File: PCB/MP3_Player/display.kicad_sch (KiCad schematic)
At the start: 8 parts, among them Q1 S8050

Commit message: Minor Schematic Changes
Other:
- moved on the sheet: Q1, R11, R12, R13, TP11

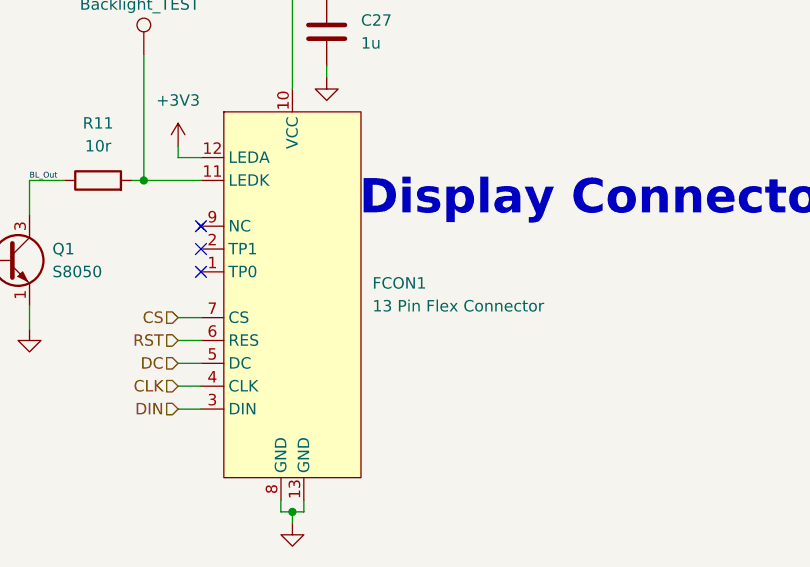
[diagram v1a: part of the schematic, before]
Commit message: Started Making BOM
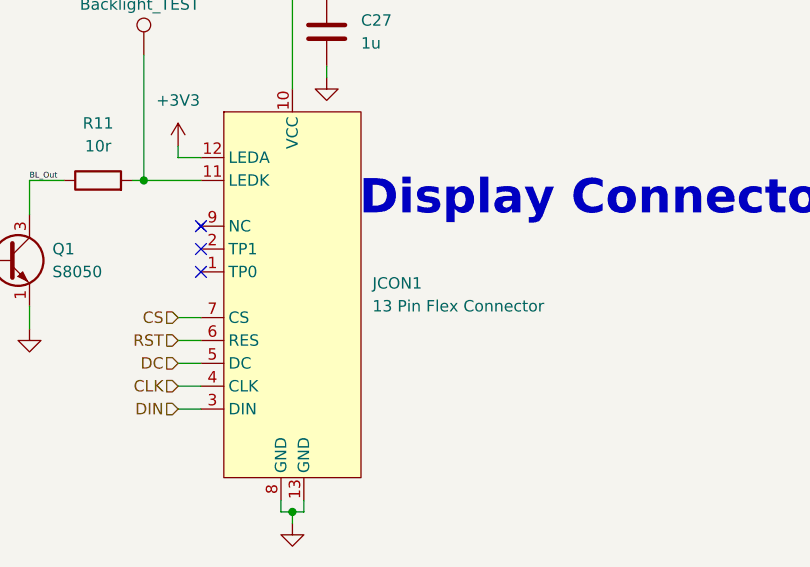
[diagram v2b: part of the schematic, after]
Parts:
- C27: Mfr. Part # (none) -> CL05A105MQ5NNND; Store URL - Digikey (none) -> https://www.digikey.pt/pt/products/detail/samsung-electro-m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; Store URL - Mouser (none) -> https://pt.mouser.com/en/ProductDetail/Samsung-Electro-Mech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
- Q1: Mfr. Part # (none) -> S8050; Store URL - Digikey (none) -> https://www.digikey.pt/pt/products/detail/guangdong-inmark-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
- TP11: now left out of the parts list
- renumbered FCON1 to JCON1

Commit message: Continue Making BOM
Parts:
- DSP1: Mfr. Part # (none) -> TST09602A
- JCON1: Mfr. Part # (none) -> IMSA-9640S-13Y900; Store URL - Digikey (none) -> https://www.digikey.pt/pt/products/detail/iriso/IMSA-9640S-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
- Q1: footprint Package_TO_SOT_THT:TO-92_Inline -> (none); Store URL - Mouser (none) -> https://pt.mouser.com/en/ProductDetail/Comchip-Technology/S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
- R11: Mfr. Part # (none) -> CRCW060310R0FKEA; Store URL - Digikey (none) -> https://www.digikey.pt/pt/products/detail/vishay-dale/CRCW0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; Store URL - Mouser (none) -> https://pt.mouser.com/en/ProductDetail/Vishay/CRCW060310R0F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
- R12: Mfr. Part # (none) -> CRCW040210K0FKED; Store URL - Digikey (none) -> https://www.digikey.pt/pt/products/detail/vishay-dale/CRCW0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; Store URL - Mouser (none) -> https://pt.mouser.com/en/ProductDetail/Vishay/CRCW040210K0F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
- R13: Mfr. Part # (none) -> CRCW04021K00FKED; Store URL - Digikey (none) -> https://www.digikey.pt/pt/products/detail/vishay-dale/CRCW0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; Store URL - Mouser (none) -> https://pt.mouser.com/en/ProductDetail/Vishay/CRCW04021K00F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
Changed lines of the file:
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@@
 			)
 		)
-		(property "Datasheet" ""
+		(property "Datasheet" "https://www.panelook.com/TST09602A-0-96inch-IPS-TFT-LCD-screen-80-160-350cd-m-sup2-13PINS-SPI-ST7735S-Wearable-LCD-detail_134063.html"
 			(at 77.47 133.35 0)
 			(hide yes)
@@
 			)
 		)
-		(property "Description" ""
+		(property "Description" "0.96 inch IPS TFT LCD screen 80x160 350cd/m² 13PINS SPI ST7735S"
 			(at 77.47 137.16 0)
 			(hide yes)
@@
 		)
 		(property "Store URL - TME" ""
+			(at 77.47 137.16 0)
+			(hide yes)
+			(show_name no)
+			(do_not_autoplace no)
+			(effects
+				(font
+					(size 1.27 1.27)
+				)
+			)
+		)
+		(property "Mfr. Part #" "TST09602A"
 			(at 77.47 137.16 0)
 			(hide yes)
@@
 			)
 		)
-		(property "Datasheet" ""
+		(property "Datasheet" "https://www.irisoconnectors.com/system/cms/assets/uploads/files/spec-sheets/product/original/is-9640a-1.pdf?1543584151"
 			(at 154.94 100.33 0)
 			(hide yes)
@@
 			)
 		)
-		(property "Description" "0.96 inch IPS TFT LCD screen 80x160 350cd/m² 13PINS SPI ST7735S"
+		(property "Description" "13 Pin 0.4mm Pitch"
 			(at 156.464 135.89 0)
 			(hide yes)
@@
 		)
 		(property "Store URL - TME" ""
+			(at 154.94 100.33 0)
+			(hide yes)
+			(show_name no)
+			(do_not_autoplace no)
+			(effects
+				(font
+					(size 1.27 1.27)
+				)
+			)
+		)
+		(property "Mfr. Part #" "IMSA-9640S-13Y900"
+			(at 154.94 100.33 0)
+			(hide yes)
+			(show_name no)
+			(do_not_autoplace no)
+			(effects
+				(font
+					(size 1.27 1.27)
+				)
+			)
+		)
+		(property "Store URL - Digikey" "https://www.digikey.pt/pt/products/detail/iriso/IMSA-9640S-13Y900/26774114"
 			(at 154.94 100.33 0)
 			(hide yes)
@@
 			)
 		)
-		(property "Datasheet" ""
+		(property "Datasheet" "https://www.vishay.com/docs/20035/dcrcwe3.pdf"
 			(at 114.3 90.17 0)
 			(hide yes)
@@
 			)
 		)
-		(property "Description" "Resistor"
+		(property "Description" "0402"
 			(at 114.3 90.17 0)
 			(hide yes)
@@
 		)
 		(property "Store URL - TME" ""
+			(at 114.3 90.17 0)
+			(hide yes)
+			(show_name no)
+			(do_not_autoplace no)
+			(effects
+				(font
+					(size 1.27 1.27)
+				)
+			)
+		)
+		(property "Mfr. Part #" "CRCW040210K0FKED"
+			(at 114.3 90.17 0)
+			(hide yes)
+			(show_name no)
+			(do_not_autoplace no)
+			(effects
+				(font
+					(size 1.27 1.27)
+				)
+			)
+		)
+		(property "Store URL - Digikey" "https://www.digikey.pt/pt/products/detail/vishay-dale/CRCW040210K0FKED/1178121"
+			(at 114.3 90.17 0)
+			(hide yes)
+			(show_name no)
+			(do_not_autoplace no)
+			(effects
+				(font
+					(size 1.27 1.27)
+				)
+			)
+		)
+		(property "Store URL - Mouser" "https://pt.mouser.com/en/ProductDetail/Vishay/CRCW040210K0FKED?qs=rlE3Te1NifyN3e8vvxacSw%3D%3D"
 			(at 114.3 90.17 0)
 			(hide yes)
@@
 			)
 		)
-		(property "Footprint" "Package_TO_SOT_THT:TO-92_Inline"
+		(property "Footprint" ""
 			(at 128.27 98.425 0)
 			(hide yes)
@@
 			)
 		)
-		(property "Description" "0.7A Ic, 20V Vce, Low Voltage High Current NPN Transistor, TO-92"
+		(property "Description" "0.7A Ic, 20V Vce, Low Voltage High Current NPN Transistor, SOT-23"
 			(at 123.19 96.52 0)
 			(hide yes)
@@
 		)
 		(property "Store URL - Digikey" "https://www.digikey.pt/pt/products/detail/guangdong-inmark-electronics-co-ltd/S8050/28538968"
+			(at 123.19 96.52 0)
+			(hide yes)
+			(show_name no)
+			(do_not_autoplace no)
+			(effects
+				(font
+					(size 1.27 1.27)
+				)
+			)
+		)
+		(property "Store URL - Mouser" "https://pt.mouser.com/en/ProductDetail/Comchip-Technology/SS8050-G?qs=LLUE9lz1YbcHg%252BWLMAtcrQ%3D%3D"
 			(at 123.19 96.52 0)
 			(hide yes)
@@
 			)
 		)
-		(property "Datasheet" ""
+		(property "Datasheet" "https://www.vishay.com/docs/20035/dcrcwe3.pdf"
 			(at 102.87 96.52 0)
 			(hide yes)
@@
 			)
 		)
-		(property "Description" "Resistor"
+		(property "Description" "0402"
 			(at 102.87 96.52 0)
 			(hide yes)
@@
 		)
 		(property "Store URL - TME" ""
+			(at 102.87 96.52 90)
+			(hide yes)
+			(show_name no)
+			(do_not_autoplace no)
+			(effects
+				(font
+					(size 1.27 1.27)
+				)
+			)
+		)
+		(property "Mfr. Part #" "CRCW04021K00FKED"
+			(at 102.87 96.52 90)
+			(hide yes)
+			(show_name no)
+			(do_not_autoplace no)
+			(effects
+				(font
+					(size 1.27 1.27)
+				)
+			)
+		)
+		(property "Store URL - Digikey" "https://www.digikey.pt/pt/products/detail/vishay-dale/CRCW04021K00FKED/1178007"
+			(at 102.87 96.52 90)
+			(hide yes)
+			(show_name no)
+			(do_not_autoplace no)
+			(effects
+				(font
+					(size 1.27 1.27)
+				)
+			)
+		)
+		(property "Store URL - Mouser" "https://pt.mouser.com/en/ProductDetail/Vishay/CRCW04021K00FKED?qs=YX%252BK5oaHNYqQ2WK%252BIAW12A%3D%3D"
 			(at 102.87 96.52 90)
 			(hide yes)
@@
 			)
 		)
-		(property "Datasheet" ""
+		(property "Datasheet" "https://www.vishay.com/docs/20035/dcrcwe3.pdf"
 			(at 133.35 87.63 0)
 			(hide yes)
@@
 			)
 		)
-		(property "Description" "Resistor"
+		(property "Description" "0603"
 			(at 133.35 87.63 0)
 			(hide yes)
@@
 			(at 133.35 87.63 90)
 			(hide yes)
+			(show_name no)
+			(do_not_autoplace no)
+			(effects
+				(font
+					(size 1.27 1.27)
+				)
+			)
+		)
+		(property "Mfr. Part #" "CRCW060310R0FKEA"
+			(at 133.35 87.63 90)
+			(hide yes)
+			(show_name no)
+			(do_not_autoplace no)
+			(effects
+				(font
+					(size 1.27 1.27)
+				)
+			)
+		)
+		(property "Store URL - Digikey" "https://www.digikey.pt/pt/products/detail/vishay-dale/CRCW060310R0FKEA/1174440"
+			(at 133.35 87.63 90)
+			(hide yes)
+			(show_name no)
+			(do_not_autoplace no)
+			(effects
+				(font
+					(size 1.27 1.27)
+				)
+			)
+		)
+		(property "Store URL - Mouser" "https://pt.mouser.com/en/ProductDetail/Vishay/CRCW060310R0FKEA?qs=wiO5jjUX9wsETsRLGnHNyA%3D%3D"
+			(at 133.35 87.63 90)
+			(hide yes)

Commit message: Finished BOM; Started Footprint assignment
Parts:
- C27, R12, R13: footprint (none) -> Capacitor_SMD:C_0402_1005Metric
- DSP1: footprint (none) -> N/A; Store URL - Digikey (none) -> N/A; Store URL - Mouser (none) -> N/A
- JCON1: Mfr. Part # IMSA-9640S-13Y900 -> TF29-13S-0.4SH(800); Store URL - Digikey https://www.digikey.pt/pt/products/detail/iriso/IMSA-9640S-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 -> https://www.digikey.pt/pt/products/detail/hirose-electric-c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; Store URL - Mouser (none) -> https://pt.mouser.com/en/ProductDetail/Hirose-Connector/TF2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
- R11: footprint (none) -> Capacitor_SMD:C_0603_1608Metric
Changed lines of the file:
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@@
 			)
 		)
-		(property "Footprint" ""
+		(property "Footprint" "N/A"
 			(at 77.47 143.51 0)
 			(hide yes)
@@
 		)
 		(property "Mfr. Part #" "TST09602A"
+			(at 77.47 137.16 0)
+			(hide yes)
+			(show_name no)
+			(do_not_autoplace no)
+			(effects
+				(font
+					(size 1.27 1.27)
+				)
+			)
+		)
+		(property "Store URL - Digikey" "N/A"
+			(at 77.47 137.16 0)
+			(hide yes)
+			(show_name no)
+			(do_not_autoplace no)
+			(effects
+				(font
+					(size 1.27 1.27)
+				)
+			)
+		)
+		(property "Store URL - Mouser" "N/A"
 			(at 77.47 137.16 0)
 			(hide yes)
@@
 			)
 		)
-		(property "Datasheet" "https://www.irisoconnectors.com/system/cms/assets/uploads/files/spec-sheets/product/original/is-9640a-1.pdf?1543584151"
+		(property "Datasheet" "https://www.hirose.com/product/document?clcode=CL0480-0514-0-00&productname=TF29-13S-0.4SH(800)&series=TF29&documenttype=Catalog&lang=en&documentid=D167191_en"
 			(at 154.94 100.33 0)
 			(hide yes)
@@
 			)
 		)
-		(property "Mfr. Part #" "IMSA-9640S-13Y900"
+		(property "Mfr. Part #" "TF29-13S-0.4SH(800)"
 			(at 154.94 100.33 0)
 			(hide yes)
@@
 			)
 		)
-		(property "Store URL - Digikey" "https://www.digikey.pt/pt/products/detail/iriso/IMSA-9640S-13Y900/26774114"
+		(property "Store URL - Digikey" "https://www.digikey.pt/pt/products/detail/hirose-electric-co-ltd/TF29-13S-0-4SH-800/11204980?s=N4IgTCBcDaICoDEwE4C0BGAzAZVQBgDoAWbACQAoAOPPAShAF0BfIA"
+			(at 154.94 100.33 0)
+			(hide yes)
+			(show_name no)
+			(do_not_autoplace no)
+			(effects
+				(font
+					(size 1.27 1.27)
+				)
+			)
+		)
+		(property "Store URL - Mouser" "https://pt.mouser.com/en/ProductDetail/Hirose-Connector/TF29-13S-0.4SH800?qs=T3oQrply3y8YJrVVdrUYPw%3D%3D"
 			(at 154.94 100.33 0)
 			(hide yes)
@@
 			)
 		)
-		(property "Footprint" ""
+		(property "Footprint" "Capacitor_SMD:C_0402_1005Metric"
 			(at 159.7152 74.93 0)
 			(hide yes)
@@
 			)
 		)
-		(property "Footprint" ""
+		(property "Footprint" "Capacitor_SMD:C_0402_1005Metric"
 			(at 116.078 90.17 90)
 			(hide yes)
@@
 			)
 		)
-		(property "Footprint" ""
+		(property "Footprint" "Capacitor_SMD:C_0402_1005Metric"
 			(at 102.87 98.298 90)
 			(hide yes)
@@
 			)
 		)
-		(property "Footprint" ""
+		(property "Footprint" "Capacitor_SMD:C_0603_1608Metric"
 			(at 133.35 89.408 90)
 			(hide yes)

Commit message: Footprint Assingment
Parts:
- Q1: footprint (none) -> Package_TO_SOT_SMD:TSOT-23
- R11: footprint Capacitor_SMD:C_0603_1608Metric -> Resistor_SMD:R_0603_1608Metric
- R12, R13: footprint Capacitor_SMD:C_0402_1005Metric -> Resistor_SMD:R_0402_1005Metric
- TP11: footprint (none) -> TestPoint:TestPoint_Pad_D1.5mm
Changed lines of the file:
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@@
 			)
 		)
-		(property "Footprint" ""
+		(property "Footprint" "TestPoint:TestPoint_Pad_D1.5mm"
 			(at 143.51 73.66 0)
 			(hide yes)
@@
 			)
 		)
-		(property "Footprint" "Capacitor_SMD:C_0402_1005Metric"
+		(property "Footprint" "Resistor_SMD:R_0402_1005Metric"
 			(at 116.078 90.17 90)
 			(hide yes)
@@
 			)
 		)
-		(property "Footprint" ""
+		(property "Footprint" "Package_TO_SOT_SMD:TSOT-23"
 			(at 128.27 98.425 0)
 			(hide yes)
@@
 			)
 		)
-		(property "Footprint" "Capacitor_SMD:C_0402_1005Metric"
+		(property "Footprint" "Resistor_SMD:R_0402_1005Metric"
 			(at 102.87 98.298 90)
 			(hide yes)
@@
 			)
 		)
-		(property "Footprint" "Capacitor_SMD:C_0603_1608Metric"
+		(property "Footprint" "Resistor_SMD:R_0603_1608Metric"
 			(at 133.35 89.408 90)
 			(hide yes)

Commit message: Footprint Assingment Complete
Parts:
- JCON1: footprint (none) -> TF29-13S-0.4SH(800):HRS_TF29-13S-0.4SH_800_
- TP11: footprint TestPoint:TestPoint_Pad_D1.5mm -> TestPoint:TestPoint_Pad_D1.0mm
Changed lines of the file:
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@@
 			)
 		)
-		(property "Footprint" ""
+		(property "Footprint" "TF29-13S-0.4SH(800):HRS_TF29-13S-0.4SH_800_"
 			(at 154.94 100.33 0)
 			(hide yes)
@@
 			)
 		)
-		(property "Footprint" "TestPoint:TestPoint_Pad_D1.5mm"
+		(property "Footprint" "TestPoint:TestPoint_Pad_D1.0mm"
 			(at 143.51 73.66 0)
 			(hide yes)

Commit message: PCB Routing
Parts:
- DSP1: Mfr. Part # TST09602A -> (none)
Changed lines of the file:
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@@
 			)
 		)
-		(property "Datasheet" "https://www.panelook.com/TST09602A-0-96inch-IPS-TFT-LCD-screen-80-160-350cd-m-sup2-13PINS-SPI-ST7735S-Wearable-LCD-detail_134063.html"
+		(property "Datasheet" ""
 			(at 77.47 133.35 0)
 			(hide yes)
@@
 			)
 		)
-		(property "Description" "0.96 inch IPS TFT LCD screen 80x160 350cd/m² 13PINS SPI ST7735S"
+		(property "Description" ""
 			(at 77.47 137.16 0)
 			(hide yes)
@@
 			)
 		)
-		(property "Mfr. Part #" "TST09602A"
+		(property "Mfr. Part #" ""
 			(at 77.47 137.16 0)
 			(hide yes)

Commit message: Final PCB Routing
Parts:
- removed JCON1: 13 Pin Flex Connector, TF29-13S-0.4SH(800):HRS_TF29-13S-0.4SH_800_, symbol TST09602A:TST09602A
- added FCON1: 26 Pins 0.5mm, Connector_FFC-FPC:Amphenol_F32R-1A7x1-11025_1x25-1MP_P0.5mm_Horizontal, symbol ER-TFT1.44-1:ER-TFT1.44-1
- DSP1: value TST09602A -> ER-TFT1.44-1; Mfr. Part # (none) -> ER-TFT1.44-1
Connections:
- net +3V3: now also FCON1.1 (LEDA), FCON1.20 (VDD), FCON1.21 (VDD)
- net CLK: now also FCON1.6 (DC/SCL)
- net CS: now also FCON1.5 (~{CS})
- net DC: now also FCON1.7 (~{WR}/DC)
- net DIN: now also FCON1.10 (DB0)
- net GND: now also FCON1.18 (SPI4W), FCON1.19 (IM2), FCON1.22 (GND), FCON1.3 (GND), FCON1.8 (~{RD})
- net RST: now also FCON1.9 (~{RST})
- net BL_LEDK: now reaches R11.2, TP11.1
- net BL_LEDK: now also FCON1.2 (LEDK)
- no-connect marks 3 -> 8
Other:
- moved on the sheet: C27, Q1, R11, R12, R13, TP11
